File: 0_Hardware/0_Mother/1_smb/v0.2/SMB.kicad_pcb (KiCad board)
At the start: 2 copper layers, 100 x 86 mm, 99 parts, among them IC1 MAX485, IC101 ATMEGA1284-A, IC2 DS2482-100S, J101 RJ45, J102 RTS_RESET, J103 ICSP, J104 SERIAL_REV, J202 USD_CONN, J401 HR911105_RJ45, P1 CONN_2, P101 I2C_CONN, P102 CONN_10X2, P103 CONN_5, P105 CONN_5, P107 CONN_3, P108 CONN_5, P109 CONN_3, P110 CONN_3, P112 CONN_3, P2 CONN_3, P301 CONN_2, SW101 SKQGAKE010, U201 ENC28J60, U202 LM1117IMP-3.3, U301 74HC08, U302 MP2562DS, U303 74HC08, X101 20MHz, X201 25MHz

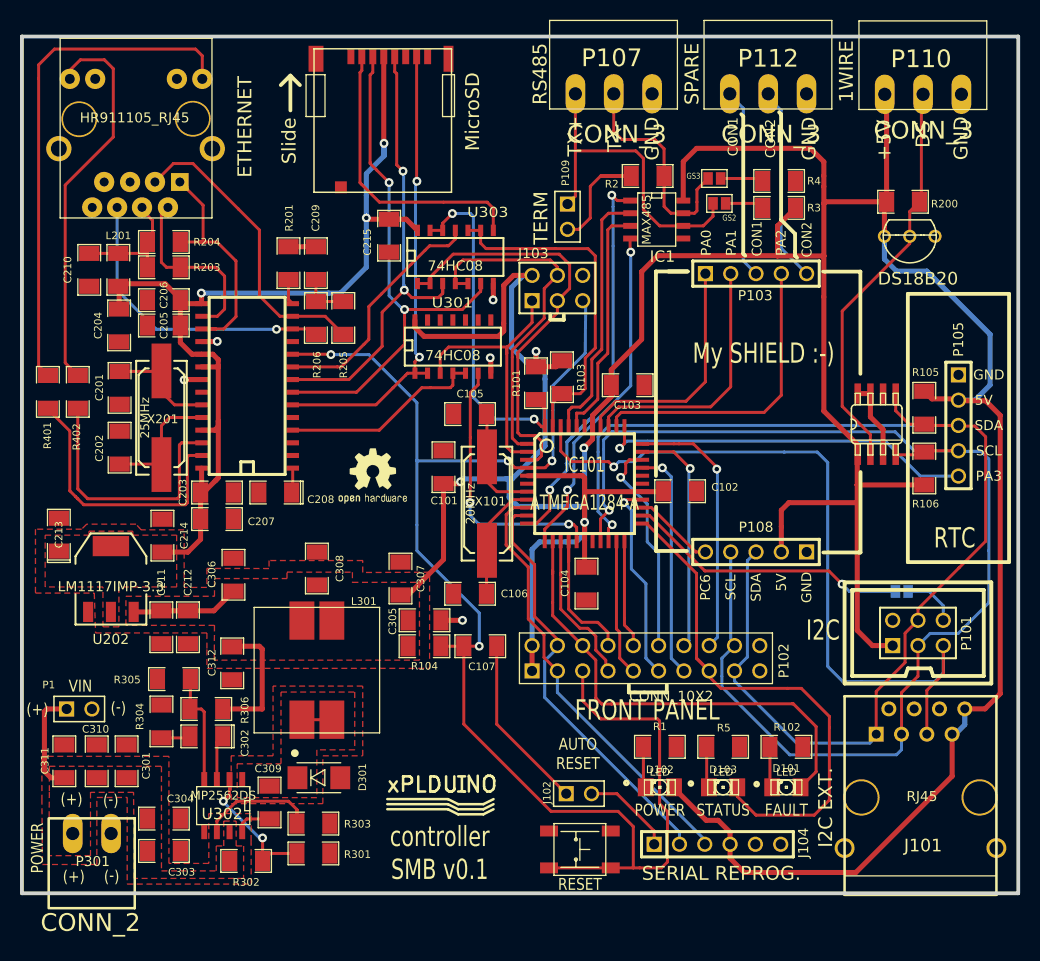
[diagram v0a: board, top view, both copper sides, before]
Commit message: mise à jour smb v0.2 (schéma, package, routage). Todo: vérifier les packages des nouveaux composants
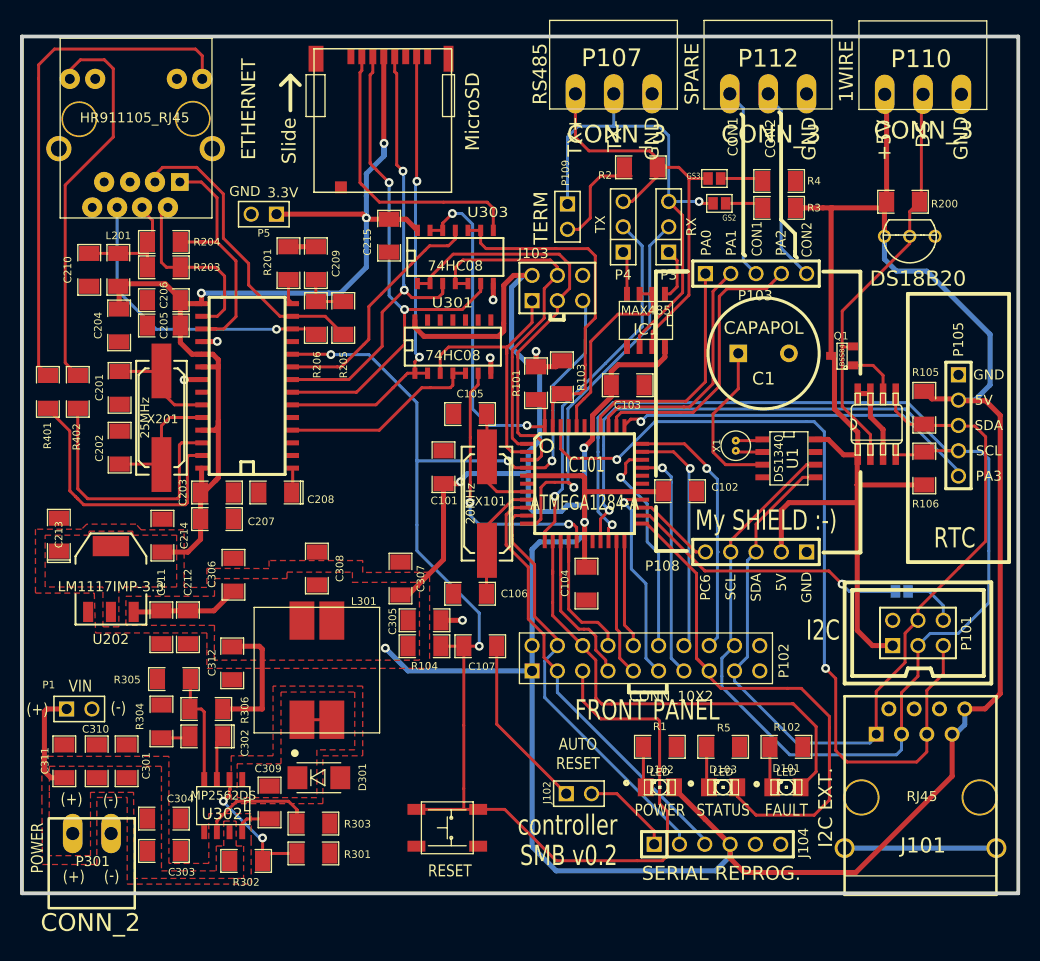
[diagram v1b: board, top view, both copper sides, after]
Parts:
- removed G***: LOGO, OSHWLOGO0.3IN
- removed logo_xplduino: VAL**, logo_xplduino
- added C1: CAPAPOL, C2V10, F.Cu at (107.4, 58.8)
- added P3: CONN_3, PIN_ARRAY_3X1, F.Cu at (97.9, 46.1)
- added P4: CONN_3, PIN_ARRAY_3X1, F.Cu at (93.3, 46.1)
- added P5: CONN_2, PIN_ARRAY_2X1, F.Cu at (57.3, 44.8)
- added Q1: BSS84, SOT23, F.Cu at (115.3, 59.1)
- added U1: DS1340, SO8E, F.Cu at (110.0, 69.3)
- added X1: CRYSTAL, quartz_0.7, F.Cu at (104.6, 68.1)
- moved SW101 13.5 mm to (75.7, 106.4), turned to 0 degrees
- moved IC1 10.2 mm to (95.6, 55.5), turned to 180 degrees
- moved R2 1.10 mm to (95.1, 40.1)
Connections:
- GS2 pad 1: TX+ -> A
- GS3 pad 1: TX- -> B
- IC1 pad 1: RX1 -> N-0000034
- IC1 pad 2: PB1 -> PB0
- IC1 pad 4: TX1 -> N-0000035
- IC1 pad 6: TX+ -> A
- IC1 pad 7: TX- -> B
- IC101 pad 41: PB1 -> (no net)
- IC2 pad 6: (no net) -> N-0000037
- J101 pad 9: (no net) -> GND
- P107 pad 2: TX- -> A
- P107 pad 3: TX+ -> B
- P109 pad 1: TX+ -> A
- R2 pad 1: TX- -> B
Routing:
- net A: track 0.00 -> 49.1 mm, vias 0 -> 1
- net B: track 0.00 -> 45.2 mm
- net TX+: track 33.0 -> 0.00 mm
- net PB1: track 25.8 -> 0.00 mm
- net TX-: track 22.7 -> 0.00 mm
- net N-0000022: track 0.00 -> 16.4 mm
- net SCL: track 128.8 -> 144.7 mm
- net GND: track 19.4 -> 34.7 mm
- net SDA: track 125.9 -> 139.6 mm
- net +5V: track 421.0 -> 430.6 mm, vias 4 -> 5
- net 3.3V: track 98.4 -> 107.6 mm
- net /INT_I2C: track 76.3 -> 85.1 mm, vias 1 -> 2
- net N-0000034: track 0.00 -> 5.34 mm
- net N-0000037: track 0.00 -> 5.26 mm
- net PB0: track 23.9 -> 19.5 mm
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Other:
- board text added: "3.3V"
- board text added: "RX"
- board text added: "SMB v0.2"
- board text added: "TX"
- board text removed: "SMB v0.1"
